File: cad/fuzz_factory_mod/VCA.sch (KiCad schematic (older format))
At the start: 22 parts

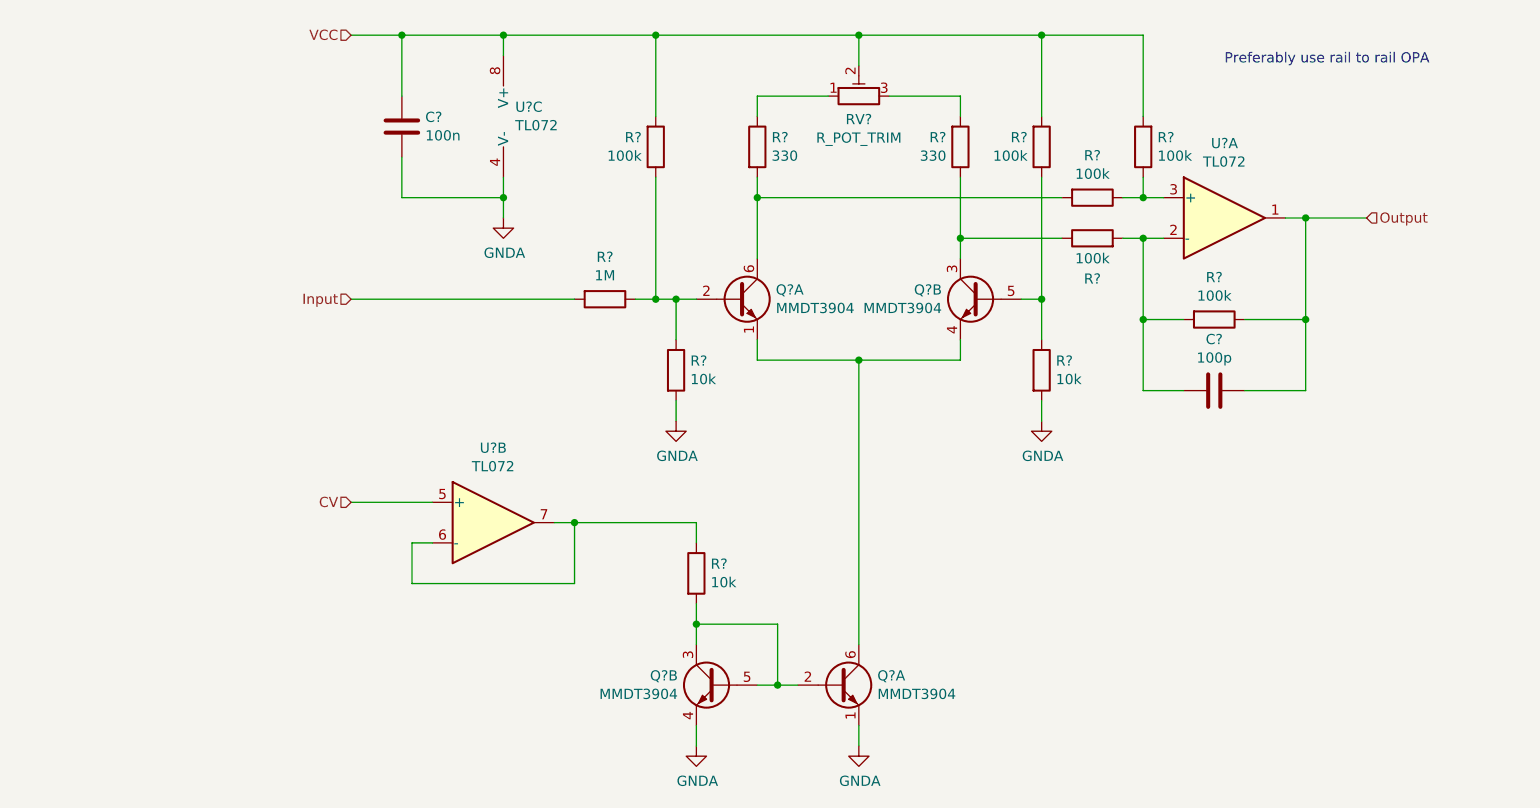
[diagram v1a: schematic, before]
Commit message: Continued schematic.
Modified fuuz_factory circuit : use of matched transistor pairs.
Added USB interface, through FT230X and direct to MCU.
Associated footprints, except for XTAL and trimmers.
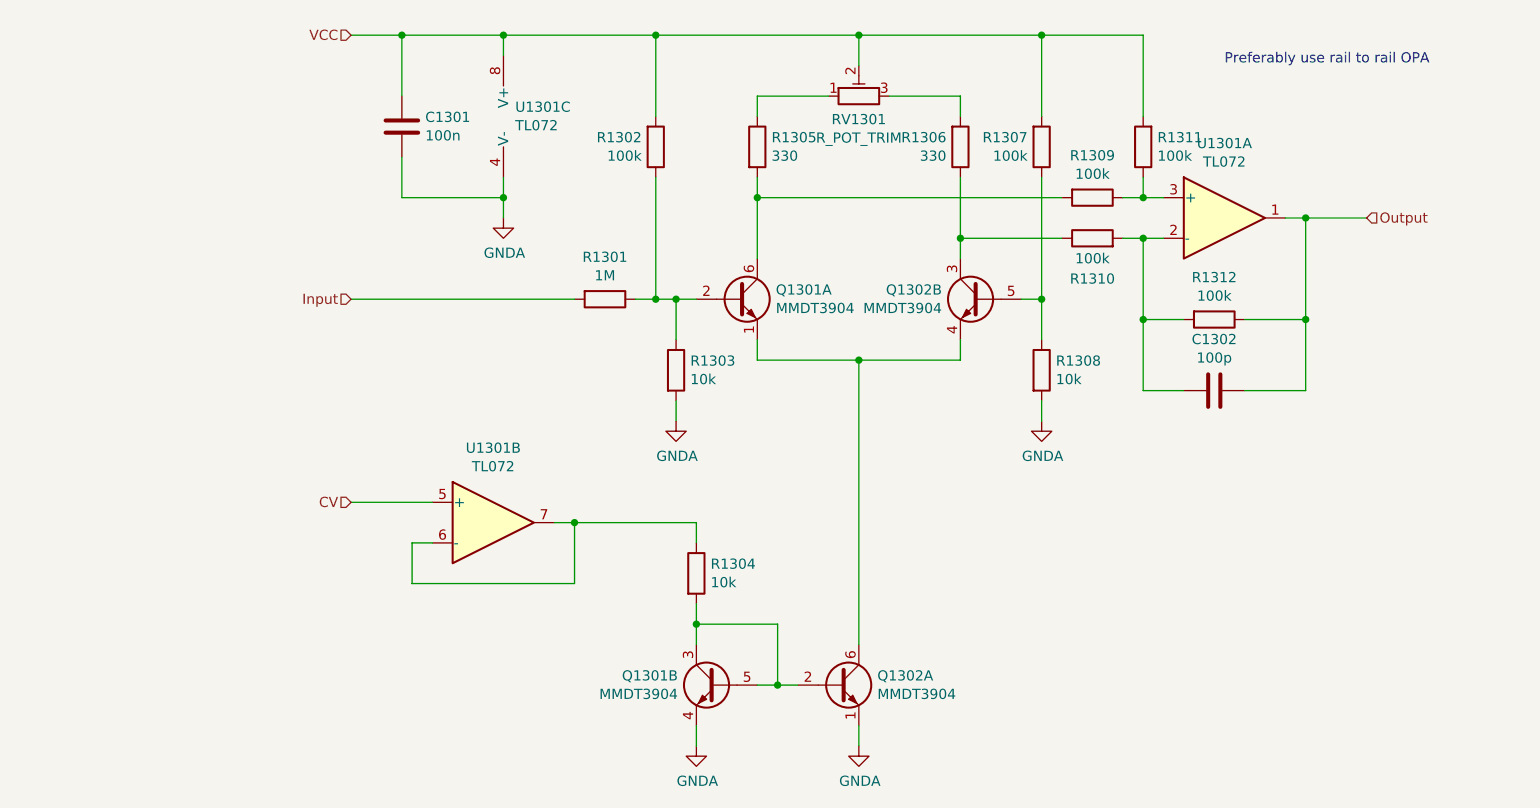
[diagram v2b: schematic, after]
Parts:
- C801, C802: renamed from C?; footprint (none) -> Capacitors_SMD:C_0603
- R801, R802, R803, R804, R805, R806, R807, R808, R809, R810, R811, R812: renamed from R?; footprint (none) -> Resistors_SMD:R_0603
- U801: renamed from U?; footprint (none) -> Housings_SOIC:SOIC-8_3.9x4.9mm_Pitch1.27mm
- gave numbers to parts that had none: 3

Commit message: Continued schematic.
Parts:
- added C803: 100n, Capacitors_SMD:C_0603, symbol Device:C
- added R813: 10k, Resistors_SMD:R_0603, symbol Device:R
- Q801, Q802: footprint Package_TO_SOT_SMD:SOT-363_SC-70-6 -> TO_SOT_Packages_SMD:SOT-363_SC-70-6
- RV801: footprint (none) -> Potentiometers:Potentiometer_Trimmer_Bourns_3266X
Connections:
- net CV: now also C803.2, R813.1
- net GNDA: now also C803.1
- new net CV_PWM: R813.2
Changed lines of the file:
@@
 $Descr A4 11693 8268
 encoding utf-8
-Sheet 13 22
+Sheet 8 26
 Title ""
 Date ""
@@
 F 0 "Q1301" H 5091 3346 50  0000 L CNN
 F 1 "MMDT3904" H 5091 3255 50  0000 L CNN
-F 2 "Package_TO_SOT_SMD:SOT-363_SC-70-6" H 5100 3400 50  0001 C CNN
+F 2 "TO_SOT_Packages_SMD:SOT-363_SC-70-6" H 5100 3400 50  0001 C CNN
 F 3 "http://www.diodes.com/_files/datasheets/ds30088.pdf" H 4900 3300 50  0001 C CNN
 	1    4900 3300
@@
 F 0 "Q1302" H 6291 3346 50  0000 L CNN
 F 1 "MMDT3904" H 6291 3255 50  0000 L CNN
-F 2 "Package_TO_SOT_SMD:SOT-363_SC-70-6" H 6300 3400 50  0001 C CNN
+F 2 "TO_SOT_Packages_SMD:SOT-363_SC-70-6" H 6300 3400 50  0001 C CNN
 F 3 "http://www.diodes.com/_files/datasheets/ds30088.pdf" H 6100 3300 50  0001 C CNN
 	2    6100 3300
@@
 F 0 "Q1302" H 5591 5246 50  0000 L CNN
 F 1 "MMDT3904" H 5591 5155 50  0000 L CNN
-F 2 "Package_TO_SOT_SMD:SOT-363_SC-70-6" H 5600 5300 50  0001 C CNN
+F 2 "TO_SOT_Packages_SMD:SOT-363_SC-70-6" H 5600 5300 50  0001 C CNN
 F 3 "http://www.diodes.com/_files/datasheets/ds30088.pdf" H 5400 5200 50  0001 C CNN
 	1    5400 5200
@@
 F 0 "Q1301" H 4991 5246 50  0000 L CNN
 F 1 "MMDT3904" H 4991 5155 50  0000 L CNN
-F 2 "Package_TO_SOT_SMD:SOT-363_SC-70-6" H 5000 5300 50  0001 C CNN
+F 2 "TO_SOT_Packages_SMD:SOT-363_SC-70-6" H 5000 5300 50  0001 C CNN
 F 3 "http://www.diodes.com/_files/datasheets/ds30088.pdf" H 4800 5200 50  0001 C CNN
 	2    4800 5200
@@
 F 0 "RV1301" V 5385 2300 50  0000 C CNN
 F 1 "R_POT_TRIM" V 5294 2300 50  0000 C CNN
-F 2 "" H 5500 2300 50  0001 C CNN
+F 2 "Potentiometers:Potentiometer_Trimmer_Bourns_3266X" H 5500 2300 50  0001 C CNN
 F 3 "~" H 5500 2300 50  0001 C CNN
 	1    5500 2300
@@
 Wire Wire Line
 	3750 2000 3750 2100
-Text HLabel 3000 4300 0    50   Input ~ 0
+Text HLabel 2500 4000 0    50   Input ~ 0
 CV
 Wire Wire Line
-	3400 4300 3000 4300
+	3400 4300 3300 4300
 Text HLabel 3000 3300 0    50   Input ~ 0
 Input
@@
 Wire Wire Line
 	3750 2000 4500 2000
+$Comp
+L Device:R R813
+U 1 1 5EDF99EB
+P 2850 4300
+AR Path="/5DE4AD88/5E344810/5EDF99EB" Ref="R813"  Part="1"
+AR Path="/5DE4AD88/5E6E7BE0/5E6FDD1C/5EDF99EB" Ref="R?"  Part="1"
+AR Path="/5DE4AD88/5E6FC466/5EDF99EB" Ref="R1313"  Part="1"
+F 0 "R1313" H 2920 4346 50  0000 L CNN
+F 1 "10k" H 2920 4255 50  0000 L CNN
+F 2 "Resistors_SMD:R_0603" V 2780 4300 50  0001 C CNN
+F 3 "~" H 2850 4300 50  0001 C CNN
+	1    2850 4300
+	0    1    1    0
+$EndComp
+$Comp
+L Device:C C803
+U 1 1 5EDFAC30
+P 3100 4650
+AR Path="/5DE4AD88/5E344810/5EDFAC30" Ref="C803"  Part="1"
+AR Path="/5DE4AD88/5E6E7BE0/5E6FDD1C/5EDFAC30" Ref="C?"  Part="1"
+AR Path="/5DE4AD88/5E6FC466/5EDFAC30" Ref="C1303"  Part="1"
+F 0 "C1303" H 2985 4604 50  0000 R CNN
+F 1 "100n" H 2985 4695 50  0000 R CNN
+F 2 "Capacitors_SMD:C_0603" H 3138 4500 50  0001 C CNN
+F 3 "~" H 3100 4650 50  0001 C CNN
+	1    3100 4650
+	1    0    0    1
+$EndComp
+$Comp
+L power:GNDA #PWR0118
+U 1 1 5EDFBB48
+P 3100 4900
+AR Path="/5DE4AD88/5E344810/5EDFBB48" Ref="#PWR0118"  Part="1"
+AR Path="/5DE4AD88/5E6E7BE0/5E6FDD1C/5EDFBB48" Ref="#PWR?"  Part="1"
+AR Path="/5DE4AD88/5E6FC466/5EDFBB48" Ref="#PWR0128"  Part="1"
+F 0 "#PWR0128" H 3100 4650 50  0001 C CNN
+F 1 "GNDA" H 3105 4727 50  0000 C CNN
+F 2 "" H 3100 4900 50  0001 C CNN
+F 3 "" H 3100 4900 50  0001 C CNN
+	1    3100 4900
+	1    0    0    -1
+$EndComp
+Wire Wire Line
+	3100 4500 3100 4300
+Connection ~ 3100 4300
+Wire Wire Line
+	3100 4300 3000 4300
+Wire Wire Line
+	3100 4900 3100 4800
+Text HLabel 2500 4300 0    50   Input ~ 0
+CV_PWM
+Wire Wire Line
+	2700 4300 2500 4300
+Wire Wire Line
+	2500 4000 3300 4000
+Wire Wire Line
+	3300 4000 3300 4300
+Connection ~ 3300 4300
+Wire Wire Line
+	3300 4300 3100 4300
 $EndSCHEMATC

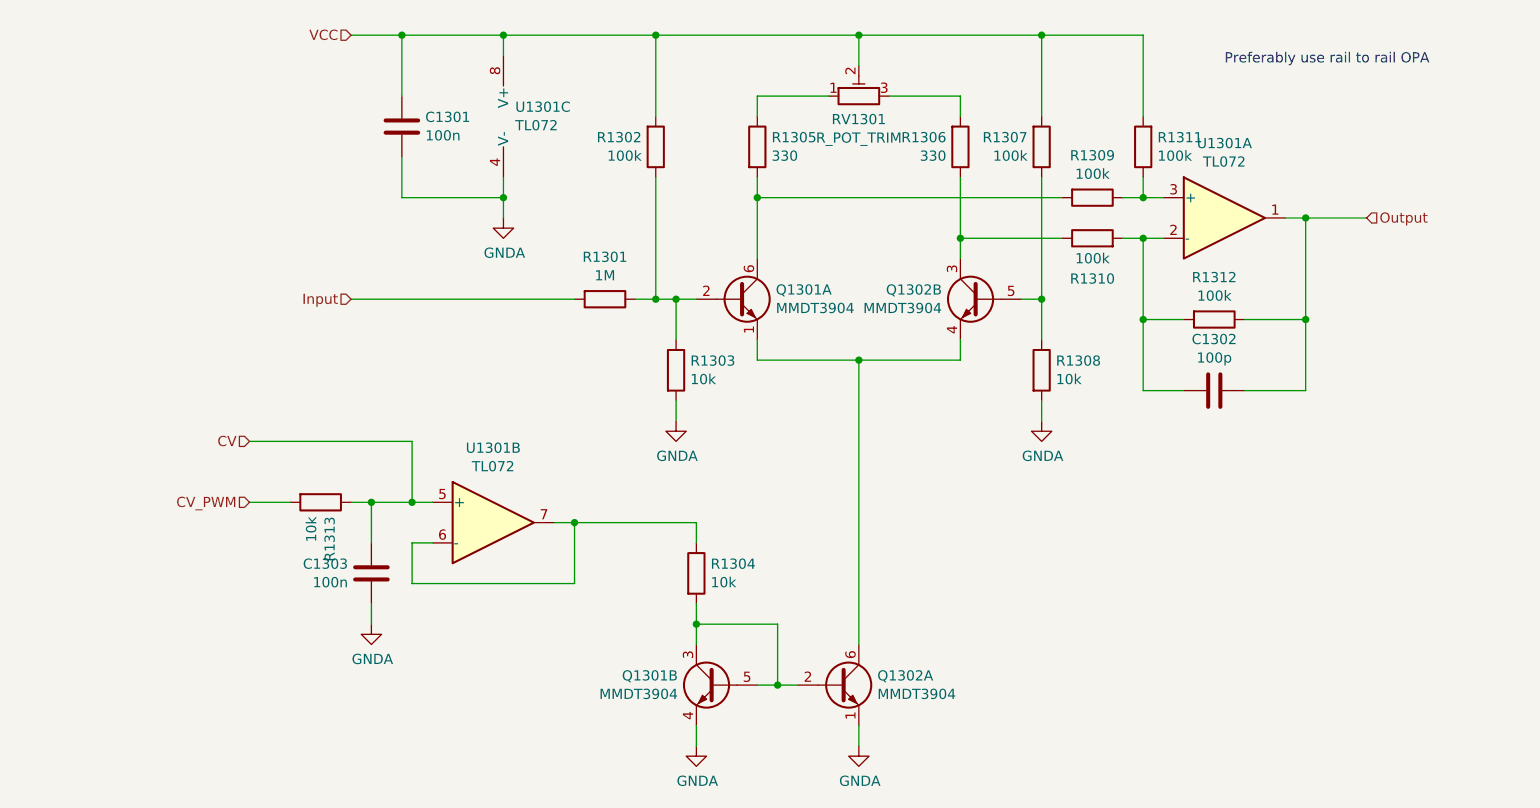
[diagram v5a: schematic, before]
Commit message: Changes architecture.
Corrections on schematic.
Continued Layout placement.
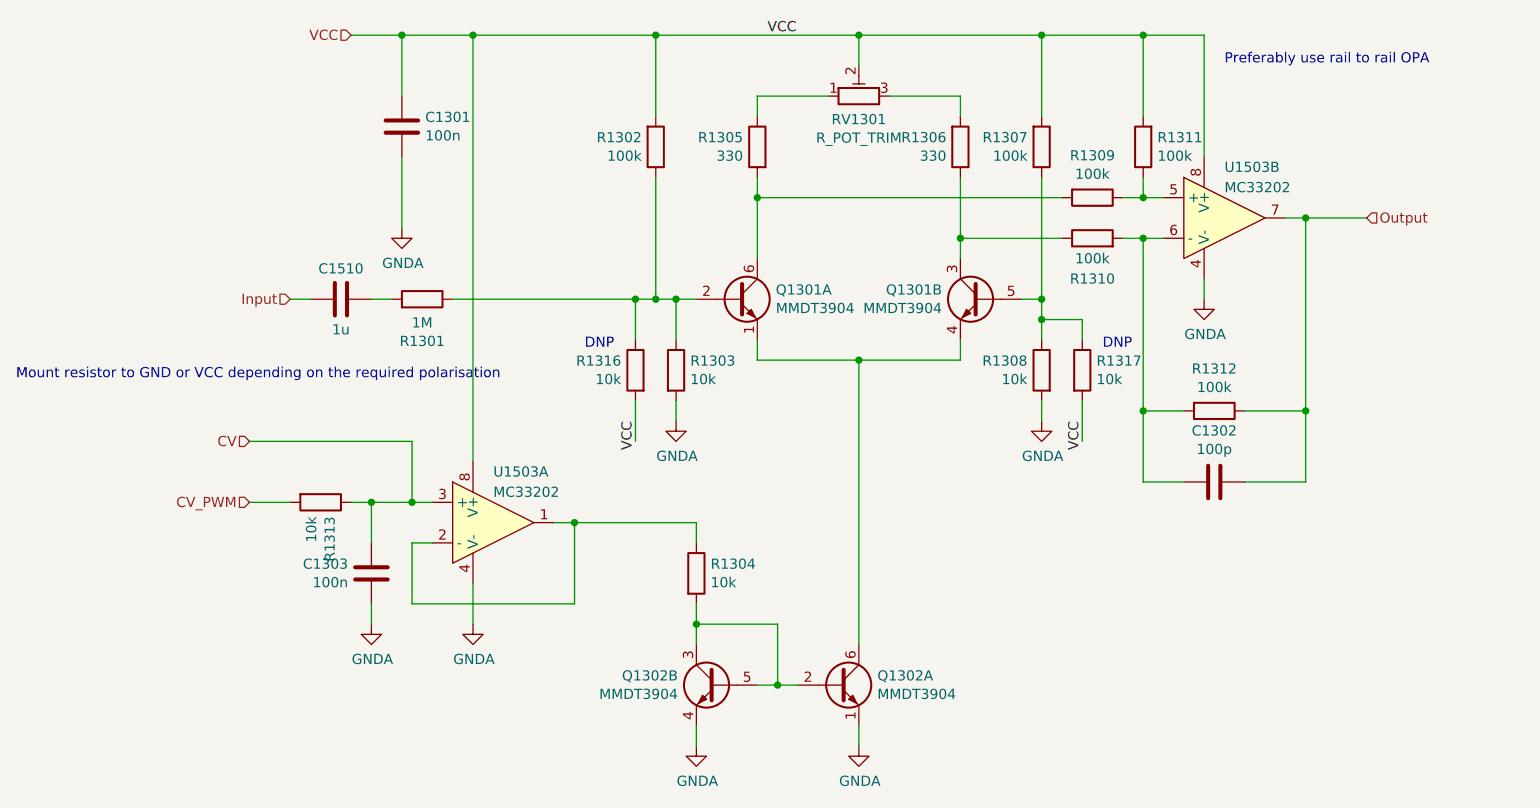
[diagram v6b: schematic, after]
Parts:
- removed U801: TL072, Housings_SOIC:SOIC-8_3.9x4.9mm_Pitch1.27mm, symbol Amplifier_Operational:TL072
- added C1510: 1u, Capacitors_SMD:C_0805, symbol Device:C
- added R814, R815: 10k, Resistors_SMD:R_0603, symbol Device:R
- added U1202: MC33202, Housings_SOIC:SOIC-8_3.9x4.9mm_Pitch1.27mm, symbol flax_lib:MC33202
- renumbered Q802 to Q801, Q801 to Q802
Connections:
- net CV: now also U1202.3 (+)
- net GNDA: now also U1202.4 (V-), U1202.4 (V-)
- net Input: now also C1510.2; no longer R801.2
- net Output: now also U1202.7
- net VCC: now also R814.2, R815.2, U1202.8 (V+), U1202.8 (V+)
- net at Q801.2 (B1), R801.1, R802.1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: now also R814.1
- net at Q801.5 (B2), R807.1, R808.1: now also R815.1
- net at R804.1: now also U1202.1, U1202.2 (-)
- net at C802.2, R810.2, R812.2: now also U1202.6 (-)
- net at R809.1, R811.1: now also U1202.5 (+)
- new net: C1510.1, R801.2
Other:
- note added: "DNP"
- note added: "Mount resistor to GND or VCC depending on the required polarisation"
- moved on the sheet: C1302, R1301, R1312

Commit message: Updated trimmers footprint.
Continued layout.
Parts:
- RV801: footprint Potentiometers:Potentiometer_Trimmer_Bourns_3266X -> Potentiometers:Potentiometer_Trimmer_Piher_PT-10v10_Horizontal_Px10.0mm_Py5.0mm
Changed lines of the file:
@@
 F 0 "RV1301" V 5385 2300 50  0000 C CNN
 F 1 "R_POT_TRIM" V 5294 2300 50  0000 C CNN
-F 2 "Potentiometers:Potentiometer_Trimmer_Bourns_3266X" H 5500 2300 50  0001 C CNN
+F 2 "Potentiometers:Potentiometer_Trimmer_Piher_PT-10v10_Horizontal_Px10.0mm_Py5.0mm" H 5500 2300 50  0001 C CNN
 F 3 "~" H 5500 2300 50  0001 C CNN
 	1    5500 2300
